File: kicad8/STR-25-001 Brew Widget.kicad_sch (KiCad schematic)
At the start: 71 parts, among them J1 USB_B_Micro, Q1 IRLML6401, Q2 FS8205A, SW1 BOOT, SW2 RESET, U1 ESP32-C3-MINI-1-N4, U2 TP4057, U3 MT3608, U4 MPU-6500, U5 MAX17048, U6 DS18B20U, U7 DW01A

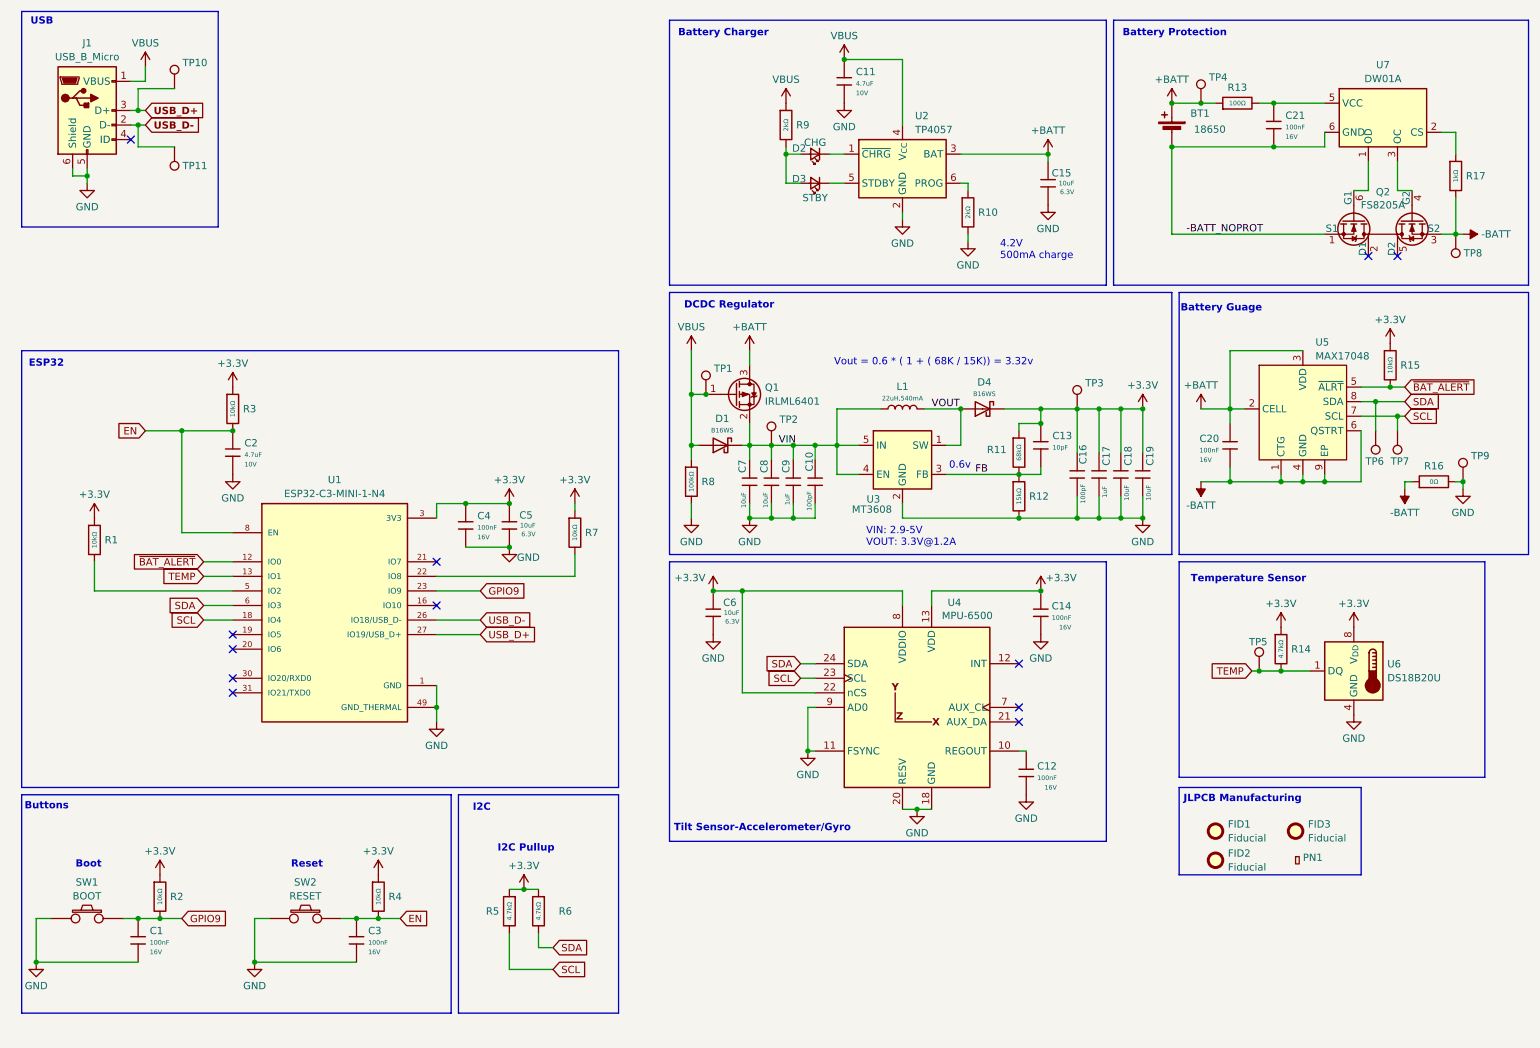
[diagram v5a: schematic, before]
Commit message: Finalising deisgn, first checks review done
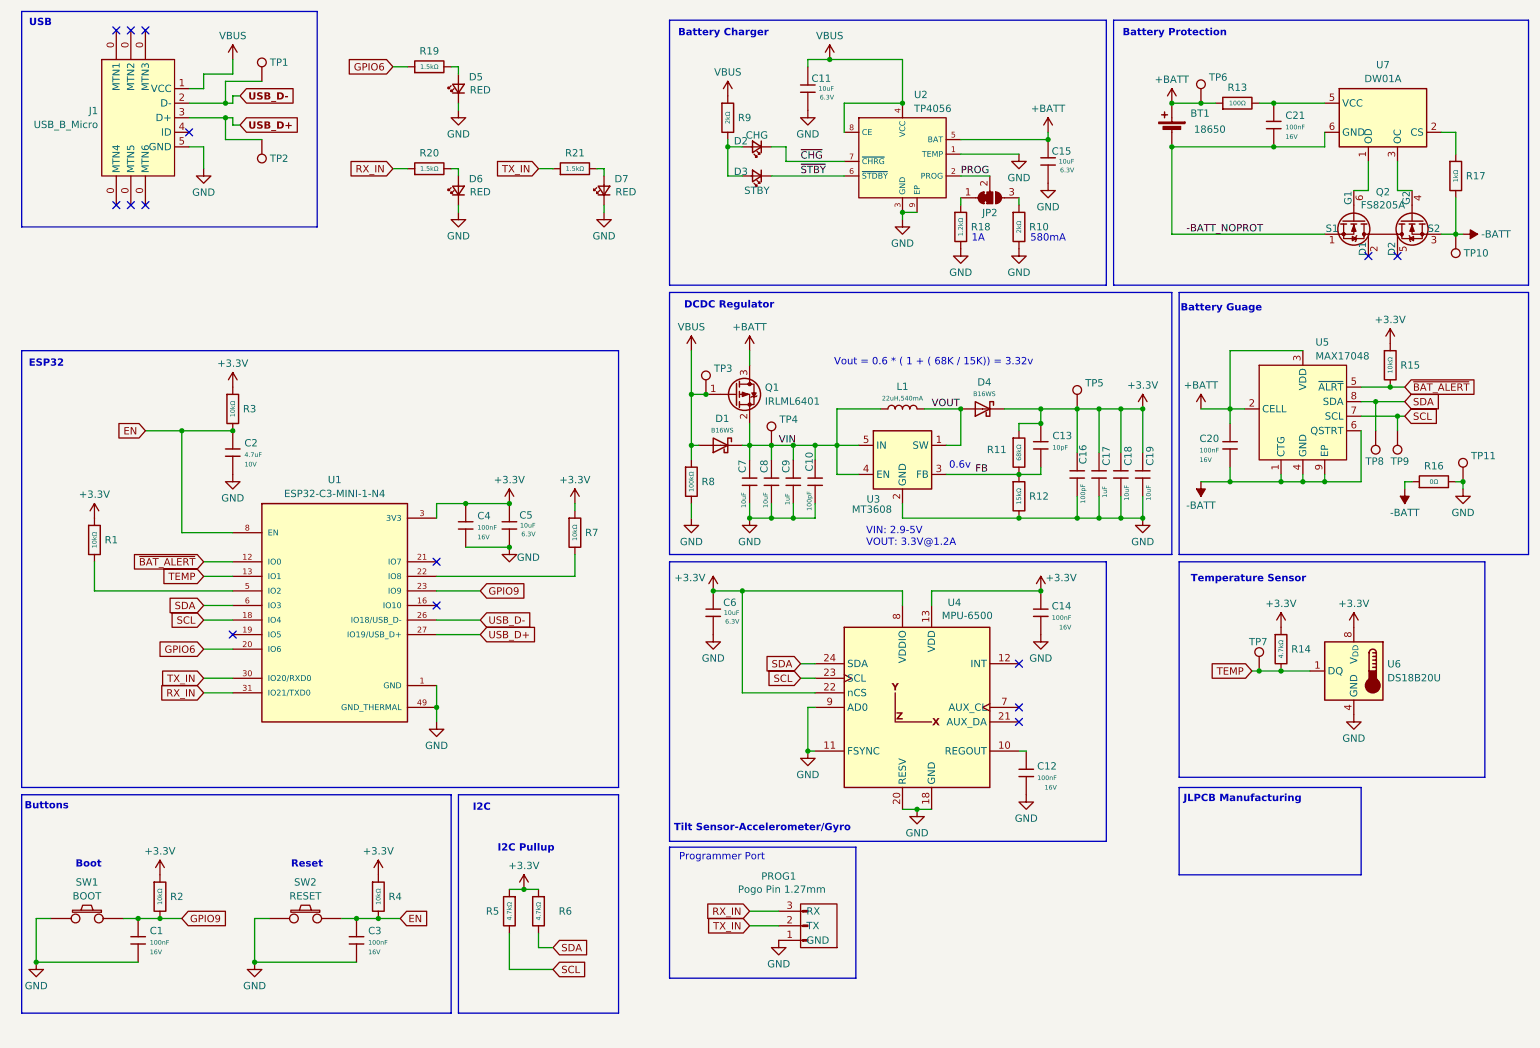
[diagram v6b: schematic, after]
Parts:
- removed C11: 4.7uF, JLCPCB-Kicad-Footprints:C_0402, symbol JLCPCB-Capacitors:0402,4.7uF
- removed FID1, FID2, FID3: Fiducial, Fiducial:Fiducial_0.5mm_Mask1mm, symbol Mechanical:Fiducial
- removed PN1: ~, JLCPCB-Kicad-Footprints:Part_Num_JLCPCB, symbol JLCPCB-Manufacturing:Part Number, JLCPCB, 0.8x0.15mm
- removed U2: TP4057, Package_TO_SOT_SMD:TSOT-23-6, symbol STR-BatteryManagement:TP4057
- added C11: 10uF, JLCPCB-Kicad-Footprints:C_0402, symbol JLCPCB-Capacitors:0402,10uF
- added D5, D6, D7: RED, LED_SMD:LED_0603_1608Metric, symbol STR-LED:Red
- added JP2: SolderJumper_3_Bridged12, Jumper:SolderJumper-3_P1.3mm_Bridged12_RoundedPad1.0x1.5mm_NumberLabels, symbol Jumper:SolderJumper_3_Bridged12
- added PROG1: Pogo Pin 1.27mm, STR-Footprints:PROG_1x3_1.27, symbol STR-Connectors:Conn_01x03_Pin_1.27mm
- added R18: 1.2kΩ, JLCPCB-Kicad-Footprints:R_0402, symbol JLCPCB-Resistors:0402,1.2kΩ
- added R19, R20, R21: 1.5kΩ, JLCPCB-Kicad-Footprints:R_0402, symbol JLCPCB-Resistors:0402,1.5kΩ
- added U2: TP4056, STR-Footprints:ESOP-8_L4.9-W3.9-P1.27-LS6.0-BL-EP, symbol STR-BatteryManagement:Battery,_Li-Ion,_1.0A,_TP4056
- J1: footprint Connector_USB:USB_Micro-B_Molex_47346-0001 -> STR-Footprints:MICRO-USB-SMD_5P_C40945; symbol STR-USB:USB_B_Micro -> STR-USB:USB_micro_B_SMD_no_holes; LCSC (none) -> C40945; LCSC Part (none) -> C40945
- L1: footprint STR-Passive:IND_LQH3NPZ220MMEL -> STR-Footprints:IND_LQH3NPZ220MMEL
- SW1, SW2: footprint STR-Switch:SW_SMD_SPST_8x3.6 -> STR-Footprints:SW_SMD_SPST_8x3.6
- U1: footprint STR-ESP32:ESP32-C3-MINI-1-N4 -> STR-Footprints:ESP32-C3-MINI-1-N4
- renumbered TP11 to TP1, TP8 to TP10, TP9 to TP11, TP10 to TP2, TP1 to TP3, TP2 to TP4, TP3 to TP5, TP4 to TP6, TP5 to TP7, TP6 to TP8, TP7 to TP9
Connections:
- net +BATT: now also U2.5 (BAT)
- net GND: now also C11.2, D5.1 (K), D6.1 (K), D7.1 (K), PROG1.1 (GND), R18.2, U2.1 (TEMP), U2.3 (GND), U2.9 (EP); no longer J1.6 (Shield)
- net VBUS: now also C11.1, U2.4 (VCC), U2.8 (CE)
- net ~{STBY}: now reaches D3.1 (K)
- net ~{STBY}: now also U2.6 (~{STDBY})
- net GPIO6: now reaches U1.20 (IO6)
- net GPIO6: now also R19.1
- net TX_IN: now reaches U1.30 (IO20/RXD0)
- net TX_IN: now also PROG1.2 (TX_IN), R21.1
- net RX_IN: now reaches U1.31 (IO21/TXD0)
- net RX_IN: now also PROG1.3 (RX_IN), R20.1
- net at R10.1: now also JP2.3 (B)
- net ~{CHG}: now reaches D2.1 (K)
- net ~{CHG}: now also U2.7 (~{CHRG})
- new net: D5.2 (A), R19.2
- new net: D6.2 (A), R20.2
- new net: JP2.1 (A), R18.1
- new net: D7.2 (A), R21.2
- new net PROG: JP2.2 (C), U2.2 (PROG)
- no-connect marks 12 -> 15
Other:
- note added: "1A"
- note added: "580mA"
- note added: "Programmer Port"
- note removed: "4.2V 500mA charge"
- moved on the sheet: C15, D2, D3, R10, R9, TP1, TP2

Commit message: BOM generated
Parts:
- D2: value CHG -> RED
- D3: value STBY -> GREEN
- PROG1, TP1, TP10, TP11, TP2, TP3, TP4, TP5, TP6, TP7, TP8, TP9: now left out of the parts list
- SW1: value BOOT -> SPST 8x3.6
- SW2: value RESET -> SPST 8x3.6
- U3: LCSC (none) -> C19189893
- U6: LCSC (none) -> C22360666
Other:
- note added: "LEDs"
- moved on the sheet: D5, D6, D7, R19, R20, R21

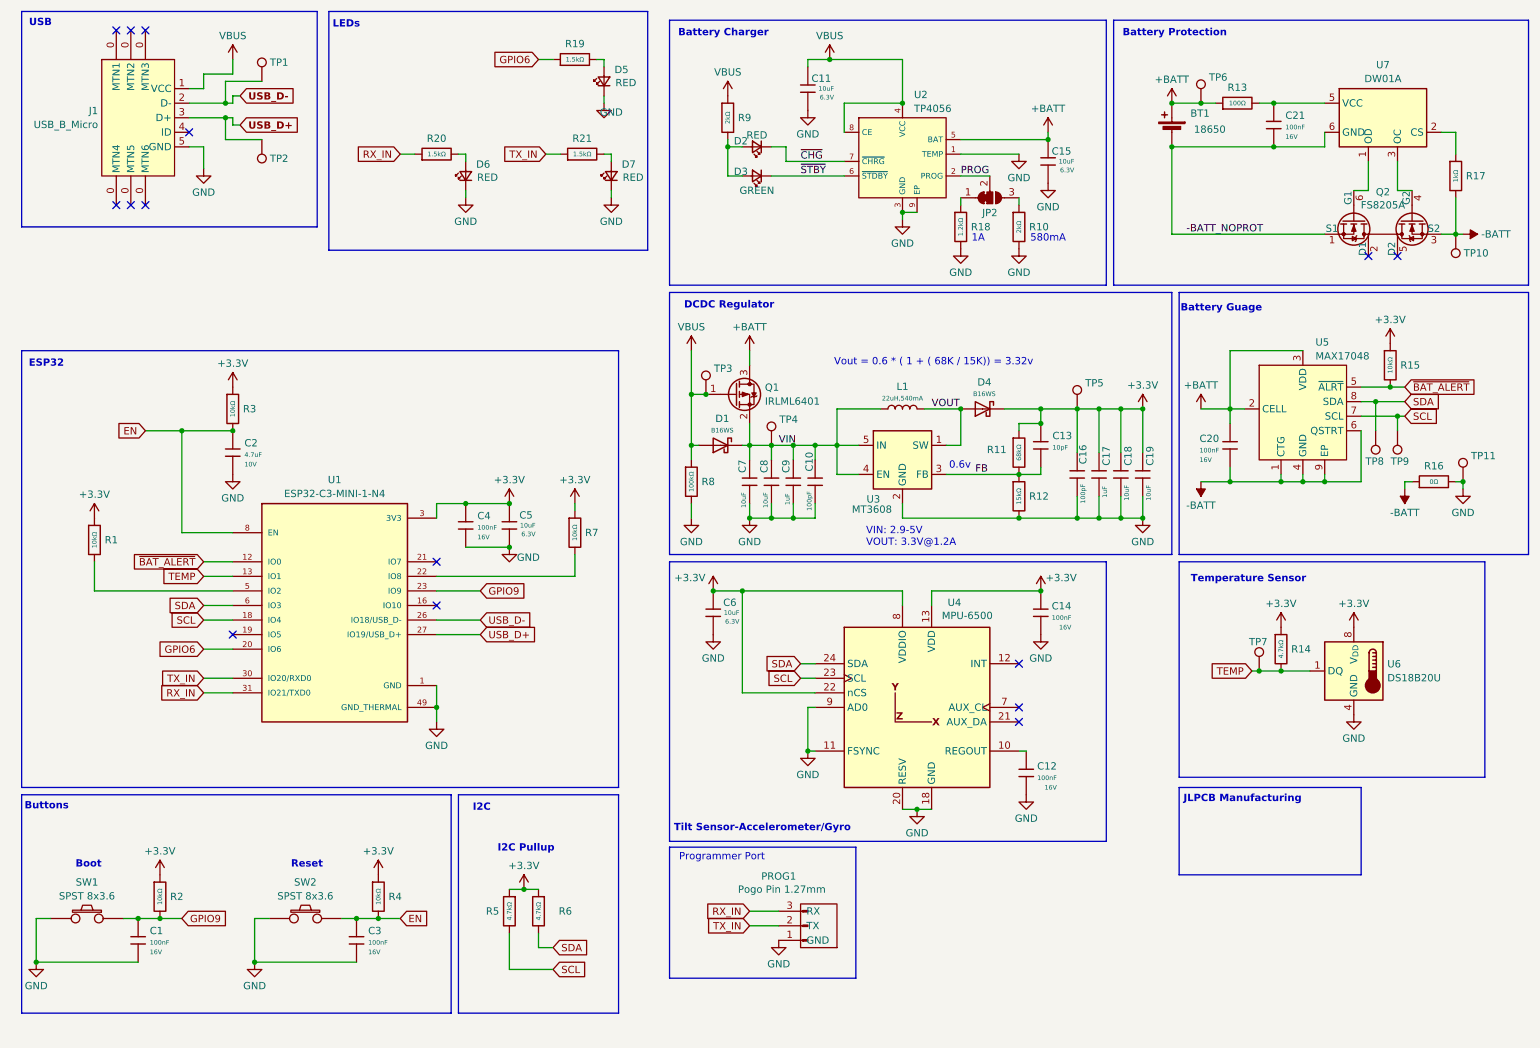
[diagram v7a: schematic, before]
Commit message: Changed to Buck Regulator using MT3406 Changed from DW01A on battery protection to AP9101C due to better low voltage protection
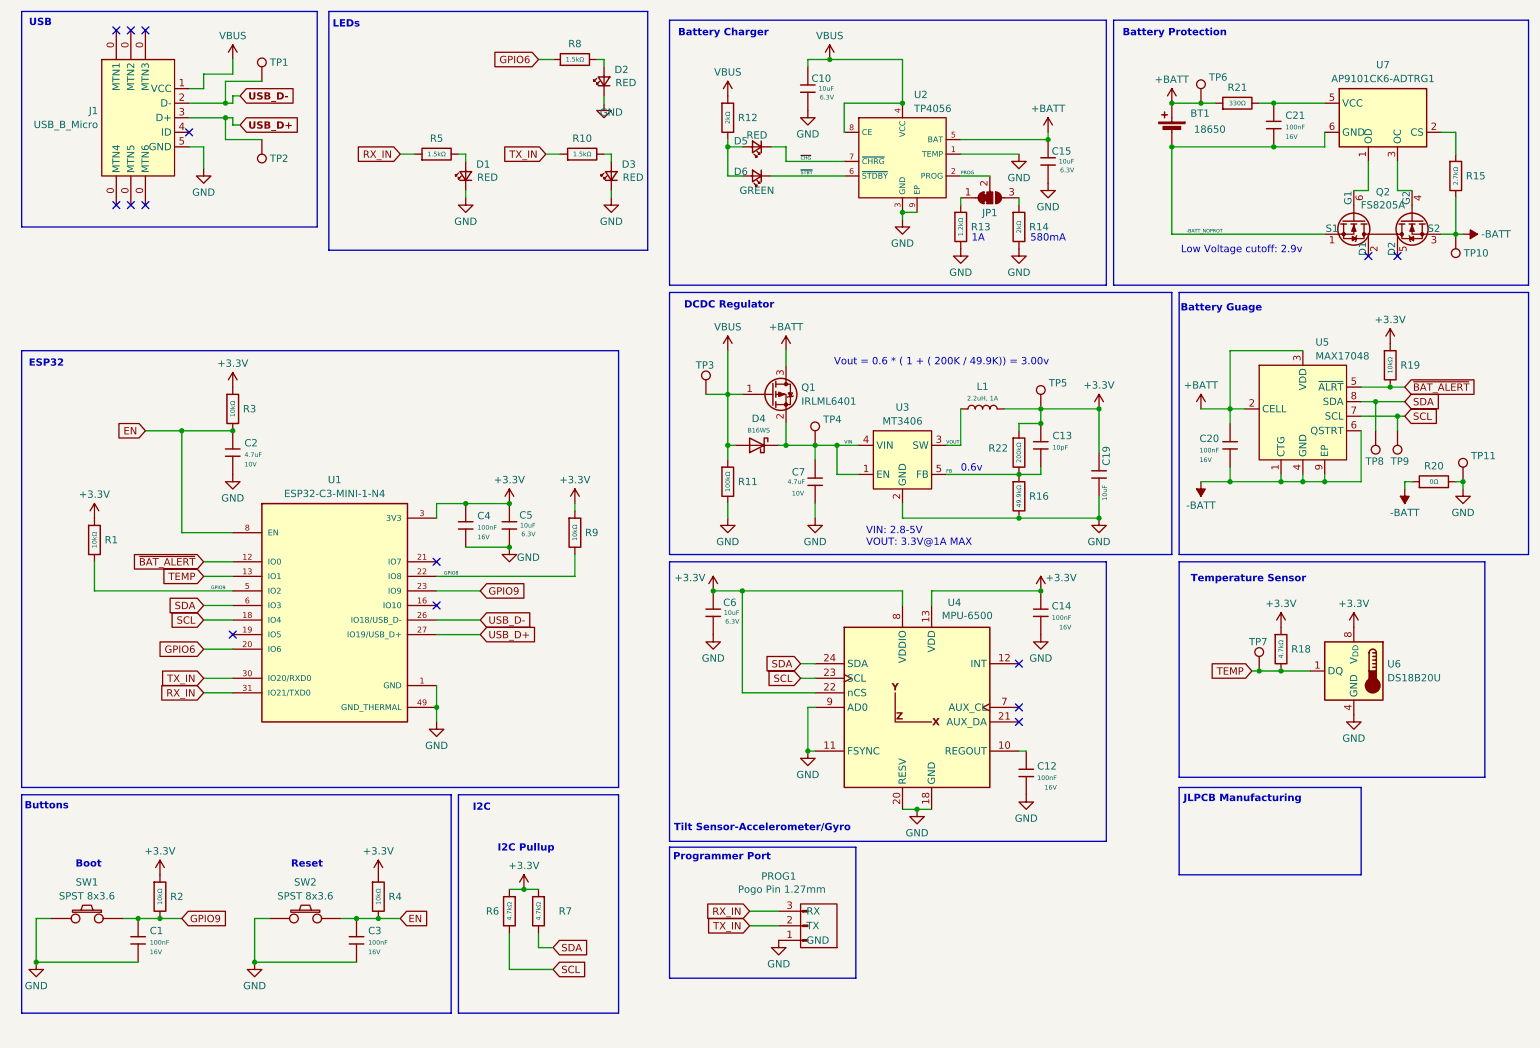
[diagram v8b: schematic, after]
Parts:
- removed C10, C16: 100pF, JLCPCB-Kicad-Footprints:C_0402, symbol JLCPCB-Capacitors:0402,100pF
- removed C17, C9: 1uF, JLCPCB-Kicad-Footprints:C_0402, symbol JLCPCB-Capacitors:0402,1uF
- removed C18, C7, C8: 10uF, JLCPCB-Kicad-Footprints:C_0402, symbol JLCPCB-Capacitors:0402,10uF
- removed D4: B16WS, JLCPCB-Kicad-Footprints:D_SOD-323, symbol JLCPCB-Diodes:Schottky,B16WS
- removed L1: 22uH,540mA, STR-Footprints:IND_LQH3NPZ220MMEL, symbol STR_Inductors:22uH,540mA
- removed R11: 68kΩ, JLCPCB-Kicad-Footprints:R_0402, symbol JLCPCB-Resistors:0402,68kΩ
- removed R12: 15kΩ, JLCPCB-Kicad-Footprints:R_0402, symbol JLCPCB-Resistors:0402,15kΩ
- removed R13: 100Ω, JLCPCB-Kicad-Footprints:R_0402, symbol JLCPCB-Resistors:0402,100Ω
- removed R16: 0Ω, JLCPCB-Kicad-Footprints:R_0402, symbol JLCPCB-Resistors:0402,0Ω
- removed R17: 1kΩ, JLCPCB-Kicad-Footprints:R_0402, symbol JLCPCB-Resistors:0402,1kΩ
- removed U3: MT3608, Package_TO_SOT_SMD:SOT-23-6, symbol Regulator_Switching:MT3608
- removed U7: DW01A, Package_TO_SOT_SMD:SOT-23-6, symbol Battery_Management:DW01A
- added C7: 4.7uF, JLCPCB-Kicad-Footprints:C_0402, symbol JLCPCB-Capacitors:0402,4.7uF
- added L1: 2.2uH, 1A, STR-Passive:IND_LQH3NPZ220MMEL, symbol STR_Inductors:2.2uH,1A
- added R15: 2.7kΩ, JLCPCB-Kicad-Footprints:R_0603, symbol JLCPCB-Resistors:0603,2.7kΩ
- added R16: 49.9kΩ, JLCPCB-Kicad-Footprints:R_0402, symbol JLCPCB-Resistors:0402,49.9kΩ
- added R20: 0Ω, JLCPCB-Kicad-Footprints:R_0805, symbol JLCPCB-Resistors:0805,0Ω
- added R21: 330Ω, JLCPCB-Kicad-Footprints:R_0603, symbol JLCPCB-Resistors:0603,330Ω
- added R22: 200kΩ, JLCPCB-Kicad-Footprints:R_0402, symbol JLCPCB-Resistors:0402,200kΩ
- added U3: MT3406, Package_TO_SOT_SMD:SOT-23-5, symbol STR-DCDC:MT3406
- added U7: AP9101CK6-ADTRG1, Package_TO_SOT_SMD:SOT-23-6, symbol STR-BatteryManagement:AP9101CK6-ADTRG1
- renumbered C11 to C10, D6 to D1, D5 to D2, D7 to D3, D1 to D4, D2 to D5, D3 to D6, JP2 to JP1, R21 to R10, R8 to R11, R9 to R12, R18 to R13, R10 to R14, R14 to R18, R15 to R19, R20 to R5, R5 to R6, R6 to R7, R19 to R8, R7 to R9
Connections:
- net +3.3V: now also L1.2, R22.1
- net +BATT: now also R21.1
- net -BATT: now also R15.2, R20.1
- net -BATT_NOPROT: now also U7.6 (GND)
- net FB: now also R16.1, R22.2, U3.5 (FB)
- net GND: now also C7.2, R16.2, R20.2, U3.2 (GND)
- net GPIO9: now also R1.2, U1.5 (IO2)
- net VIN: now also C7.1, U3.1 (EN), U3.4 (VIN)
- net VOUT: now also L1.1, U3.3 (SW)
- net at Q2.4 (G2): now also U7.3 (OC)
- net at Q2.6 (G1): now also U7.1 (OD)
- net GPIO8: now reaches R9.2, U1.22 (IO8)
- net at C21.1: now also R21.2, U7.5 (VCC)
- new net: R15.1, U7.2 (CS)
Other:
- note added: "Low Voltage cutoff: 2.9v"
- note added: "VIN: 2.8-5V VOUT: 3.3V@1A MAX"
- note added: "Vout = 0.6 * ( 1 + ( 200K / 49.9K)) = 3.00v"
- note removed: "VIN: 2.9-5V VOUT: 3.3V@1.2A"
- note removed: "Vout = 0.6 * ( 1 + ( 68K / 15K)) = 3.32v"
- moved on the sheet: C19, D4, Q1, R11, TP4, TP5
